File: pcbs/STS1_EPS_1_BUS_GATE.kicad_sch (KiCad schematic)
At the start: 0 parts

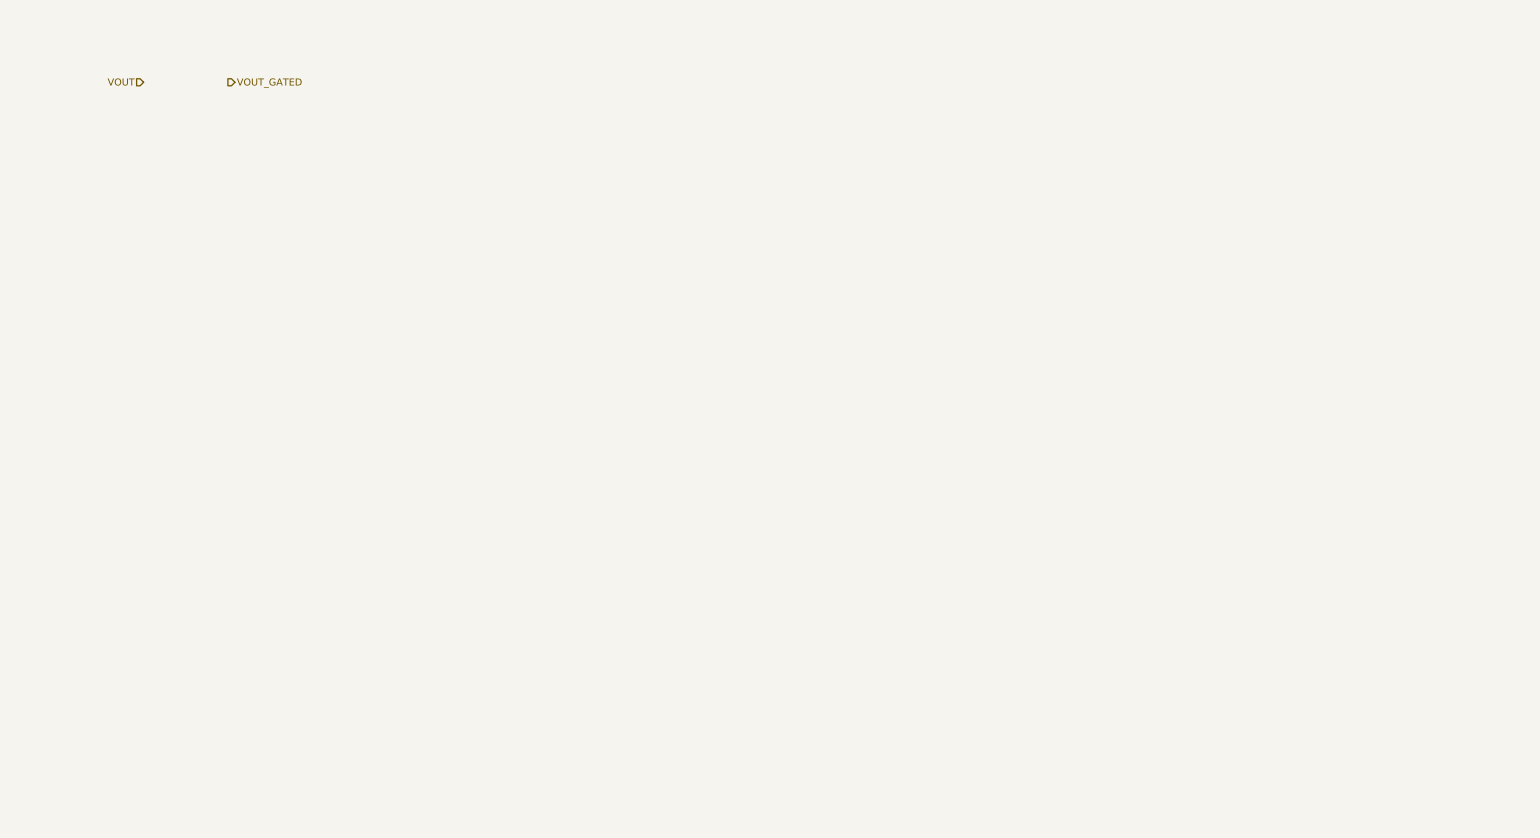
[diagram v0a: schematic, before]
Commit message: Worked on STS_EPS_1.
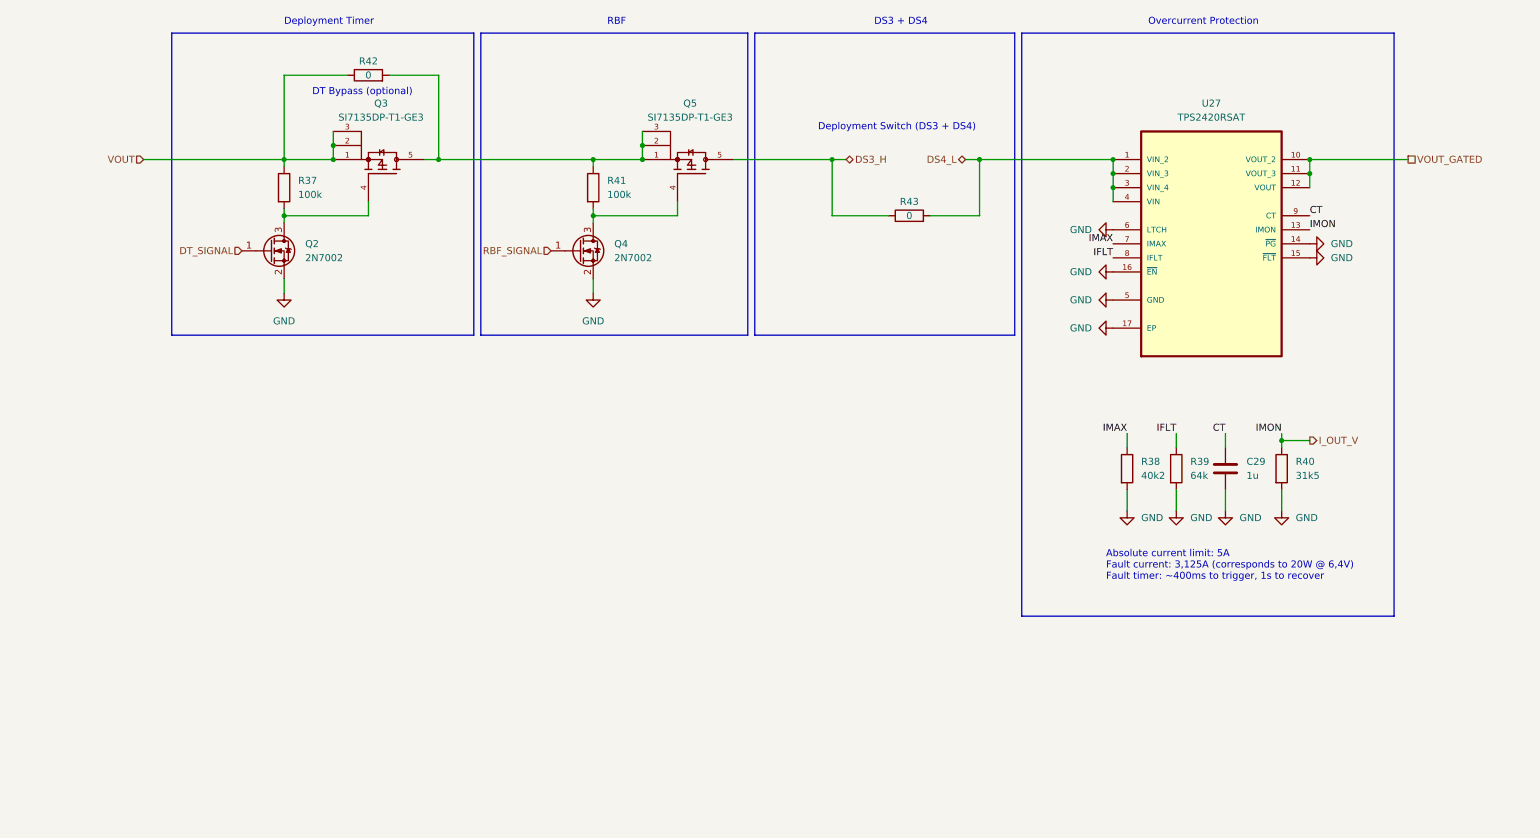
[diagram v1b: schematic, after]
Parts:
- added C29: 1u, Capacitor_SMD:C_0805_2012Metric, symbol Device:C
- added Q2, Q4: 2N7002, Package_TO_SOT_SMD:SOT-23, symbol Transistor_FET:2N7002
- added Q3, Q5: SI7135DP-T1-GE3, STS_Package_SO:POWERPAK_SO8_single, symbol STS_Transistor_FET:SI7135DP-T1-GE3
- added R37, R41: 100k, Resistor_SMD:R_0805_2012Metric, symbol Device:R
- added R38: 40k2, Resistor_SMD:R_0805_2012Metric, symbol Device:R
- added R39: 64k, Resistor_SMD:R_0805_2012Metric, symbol Device:R
- added R40: 31k5, Resistor_SMD:R_0805_2012Metric, symbol Device:R
- added R42, R43: 0, Resistor_SMD:R_0805_2012Metric, symbol Device:R
- added U27: TPS2420RSAT, Package_DFN_QFN:VQFN-16-1EP_3x3mm_P0.5mm_EP1.45x1.45mm_ThermalVias, symbol STS_Power_Management:TPS2420RSAT
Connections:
- net VOUT: now also Q3.1, Q3.2, Q3.3, R37.1, R42.1
- net VOUT_GATED: now also U27.10 (VOUT_2), U27.11 (VOUT_3), U27.12 (VOUT)
- new net: Q2.3 (D), Q3.4, R37.2
- new net: Q3.5, Q5.1, Q5.2, Q5.3, R41.1, R42.2
- new net: Q4.3 (D), Q5.4, R41.2
- new net CT: C29.1, U27.9 (CT)
- new net DS3_H: Q5.5, R43.1
- new net DS4_L: R43.2, U27.1 (VIN_2), U27.2 (VIN_3), U27.3 (VIN_4), U27.4 (VIN)
- new net DT_SIGNAL: Q2.1 (G)
- new net GND: C29.2, Q2.2 (S), Q4.2 (S), R38.2, R39.2, R40.2, U27.14 (~{PG}), U27.15 (~{FLT}), U27.16 (~{EN}), U27.17 (EP), U27.5 (GND), U27.6 (LTCH)
- new net IFLT: R39.1, U27.8 (IFLT)
- new net IMAX: R38.1, U27.7 (IMAX)
- new net I_OUT_V: R40.1, U27.13 (IMON)
- new net RBF_SIGNAL: Q4.1 (G)
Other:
- note added: "Absolute current limit: 5A Fault current: 3,125A (corresponds to 20W @ 6,4V) Fault timer: ~400ms to trigger, 1s to recover"
- note added: "DS3 + DS4"
- note added: "DT Bypass (optional)"
- note added: "Deployment Switch (DS3 + DS4)"
- note added: "Deployment Timer"
- note added: "Overcurrent Protection"
- note added: "RBF"

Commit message: Worked on STS1_EPS_1 and began work on STS1_EPS_2.
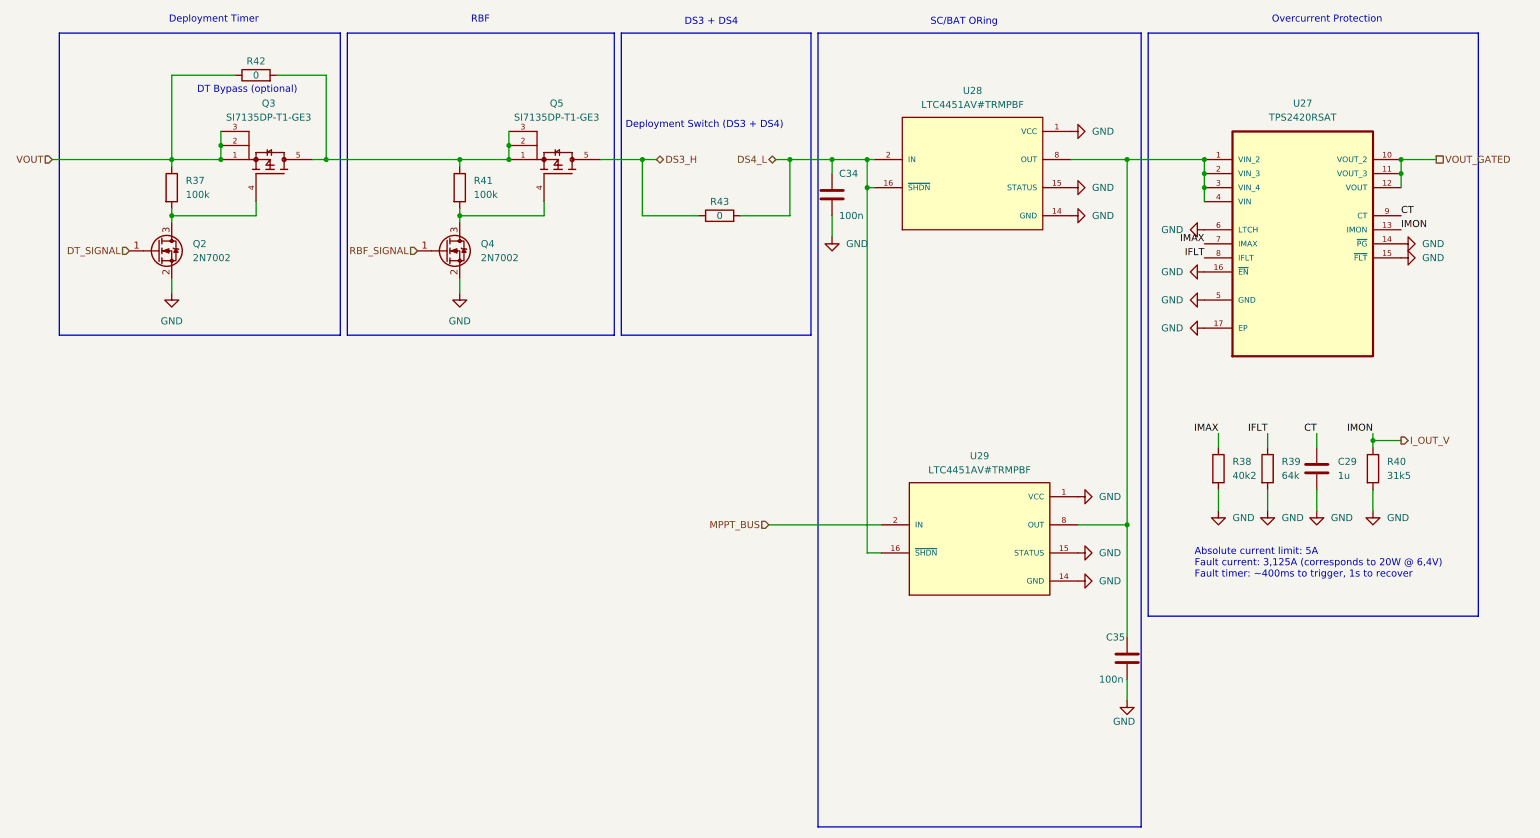
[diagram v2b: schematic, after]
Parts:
- added C34, C35: 100n, Capacitor_SMD:C_0805_2012Metric, symbol Device:C
- added U28, U29: LTC4451AV#TRMPBF, STS_Package_DFN_QFN:AD_LQFN-16, symbol STS_Power_Management:LTC4451AV#TRMPBF
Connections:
- net DS4_L: now also C34.1, U28.16 (~{SHDN}), U28.2 (IN), U29.16 (~{SHDN}); no longer U27.1 (VIN_2), U27.2 (VIN_3), U27.3 (VIN_4), U27.4 (VIN)
- net GND: now also C34.2, C35.2, U28.1 (VCC), U28.14 (GND), U28.15 (STATUS), U29.1 (VCC), U29.14 (GND), U29.15 (STATUS)
- new net: C35.1, U27.1 (VIN_2), U27.2 (VIN_3), U27.3 (VIN_4), U27.4 (VIN), U28.8 (OUT), U29.8 (OUT)
- new net MPPT_BUS: U29.2 (IN)
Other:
- note added: "SC/BAT ORing"
- moved on the sheet: C29, Q2, Q3, Q4, Q5, R37, R38, R39, R40, R41, R42, R43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
